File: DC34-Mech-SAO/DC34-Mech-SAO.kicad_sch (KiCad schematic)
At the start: 15 parts, among them J1 Conn_01x06_Male, U1 ATTINY817-MN

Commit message: Created board design.
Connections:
- net GPIO1: now also U1.16 (PB0)
- net GPIO2: now also U1.15 (PB1)
- net at R4.1: now also U1.18 (PC1); no longer U1.16 (PB0)
- net at R5.1: now also U1.19 (PC2); no longer U1.17 (PC0)
- net at R10.1: now also U1.17 (PC0); no longer U1.15 (PB1)
- net at R6.1: now also U1.20 (PC3); no longer U1.18 (PC1)
- net at R8.1: now also U1.21 (PC4); no longer U1.19 (PC2)
- net at R9.1: now also U1.22 (PC5); no longer U1.20 (PC3)
- net PWR renamed +3.3V
- no-connect marks 13 -> 11
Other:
- moved on the sheet: R10, R4, R5, R6, R8, R9

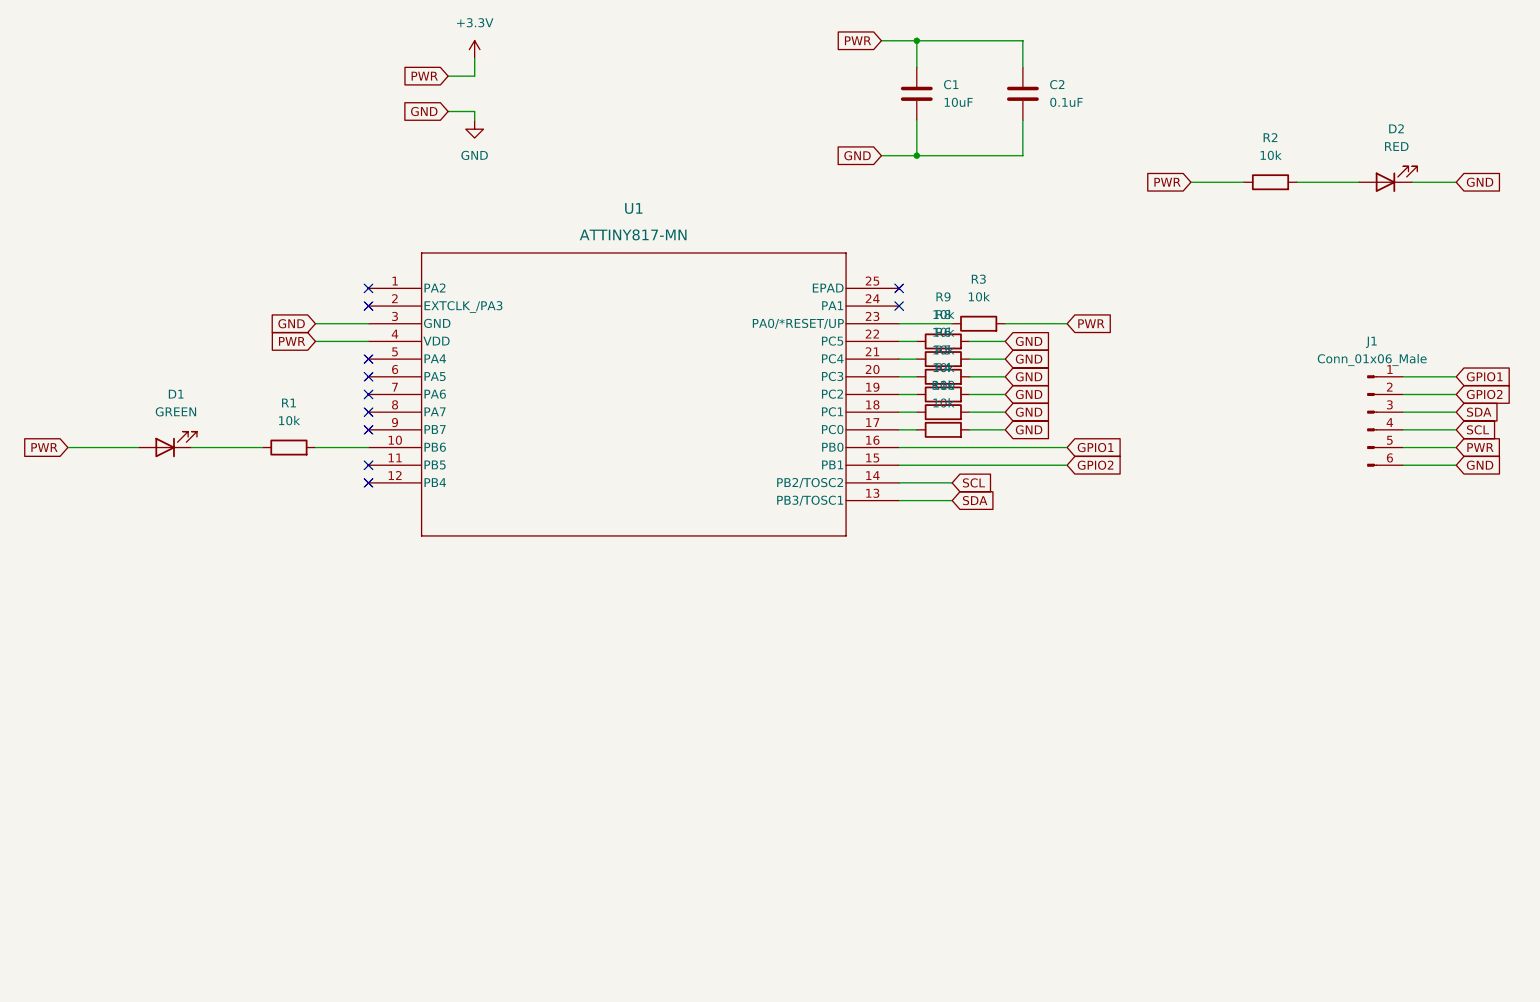
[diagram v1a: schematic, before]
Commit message: Using ATTiny 816.
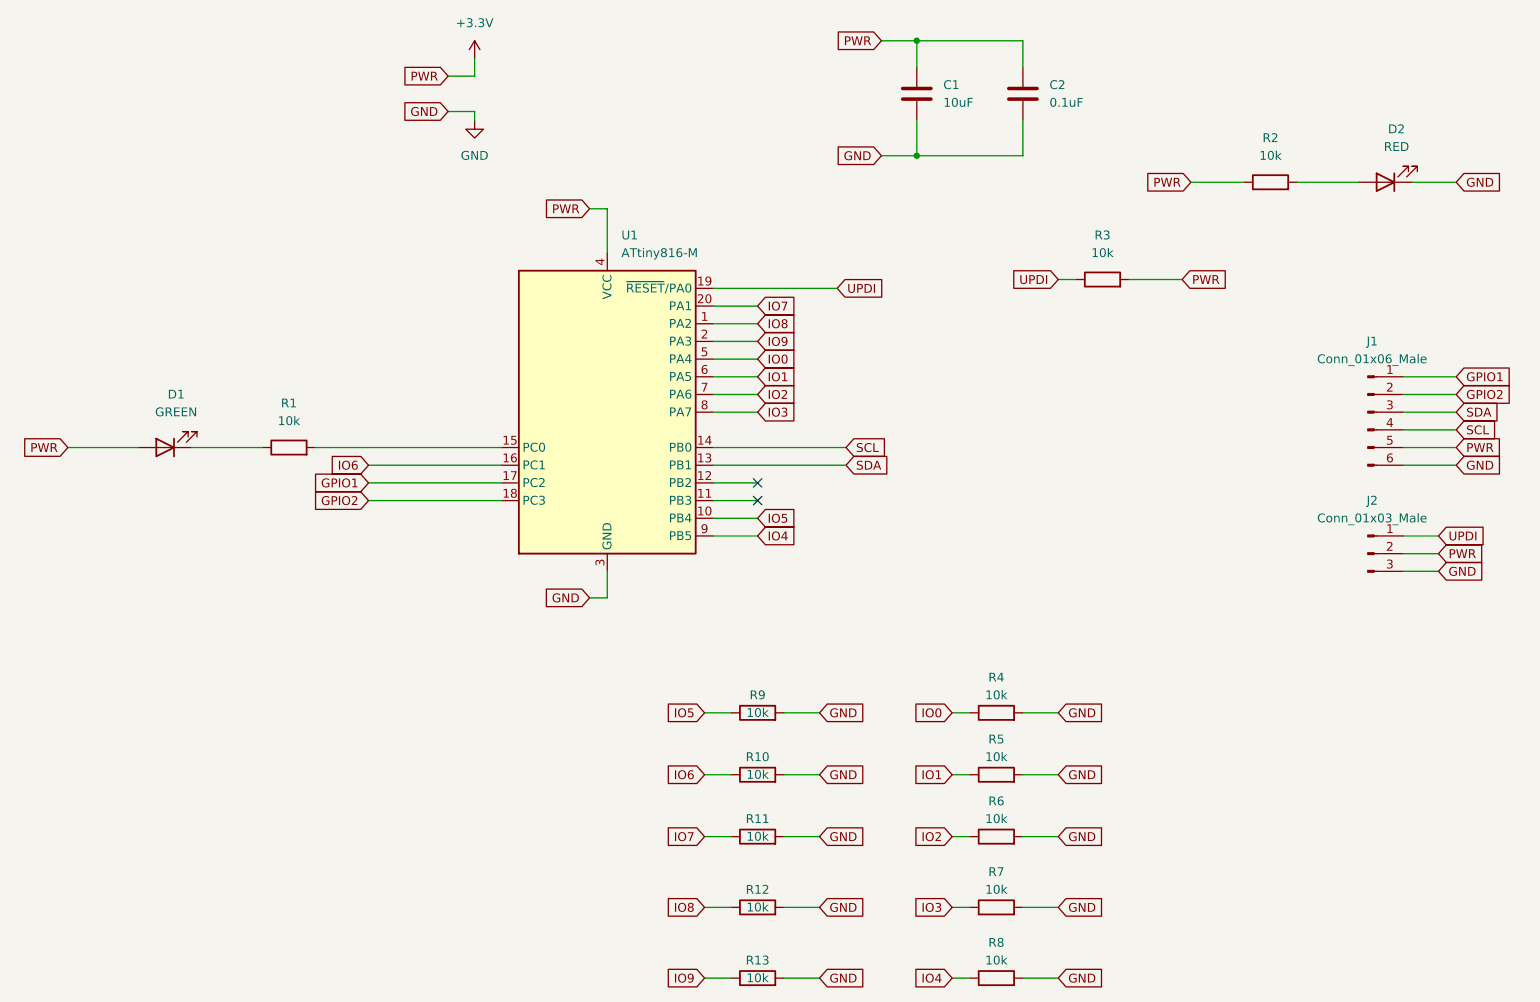
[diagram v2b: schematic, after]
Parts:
- removed U1: ATTINY817-MN, ATTINY817:QFN24_4X4MC_MCH, symbol 2026-04-14_07-41-41:ATTINY817-MN
- added J2: Conn_01x03_Male, Connector_PinSocket_2.54mm:PinSocket_1x03_P2.54mm_Vertical, symbol Connector:Conn_01x03_Male
- added R10, R11, R12, R13: 10k, Resistor_SMD:R_0402_1005Metric, symbol Device:R
- added U1: ATtiny816-M, ATTINY816:VQFN20_3X3_MCH, symbol MCU_Microchip_ATtiny:ATtiny816-M
- J1: footprint Connector_PinHeader_1.27mm:PinHeader_2x03_P1.27mm_Vertical -> Connector_PinHeader_2.54mm:PinHeader_2x03_P2.54mm_Vertical
- renumbered R8 to R7, R9 to R8, R10 to R9
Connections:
- net +3.3V: now also J2.2 (Pin_2), U1.4 (VCC)
- net GND: now also J2.3 (Pin_3), R10.2, R11.2, R12.2, R13.2, U1.21 (GND), U1.3 (GND)
- net GPIO1: now also U1.17 (PC2)
- net GPIO2: now also U1.18 (PC3)
- net SCL: now also U1.14 (PB0)
- net SDA: now also U1.13 (PB1)
- net IO0: now reaches R4.1
- net IO0: now also U1.5 (PA4)
- net IO1: now reaches R5.1
- net IO1: now also U1.6 (PA5)
- net at R1.2: now also U1.15 (PC0)
- net IO5: now reaches R9.1
- net IO5: now also U1.10 (PB4)
- net IO2: now reaches R6.1
- net IO2: now also U1.7 (PA6)
- net IO3: now reaches R7.1
- net IO3: now also U1.8 (PA7)
- net IO4: now reaches R8.1
- net IO4: now also U1.9 (PB5)
- net UPDI: now reaches R3.1
- net UPDI: now also J2.1 (Pin_1), U1.19 (~{RESET}/PA0)
- new net IO6: R10.1, U1.16 (PC1)
- new net IO7: R11.1, U1.20 (PA1)
- new net IO8: R12.1, U1.1 (PA2)
- new net IO9: R13.1, U1.2 (PA3)
- no-connect marks 11 -> 2
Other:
- moved on the sheet: R3, R4, R5, R6, R7, R8, R9

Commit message: change 2
added machine gun
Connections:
- net +3.3V: now also R4.2
- net GND: no longer R4.2
